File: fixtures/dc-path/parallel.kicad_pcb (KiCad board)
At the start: 2 copper layers, 2 parts

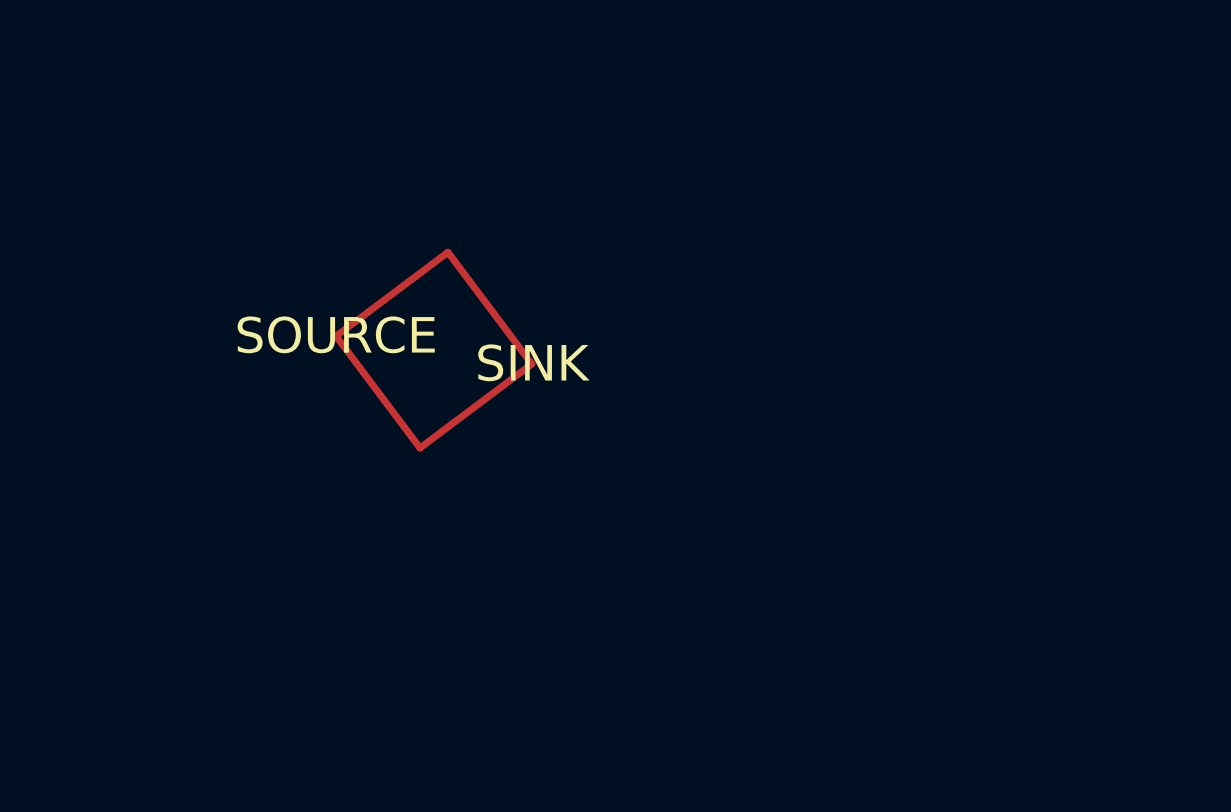
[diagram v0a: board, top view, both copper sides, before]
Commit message: Refuse DC copper outside qualified substrate and inventory footprint fields
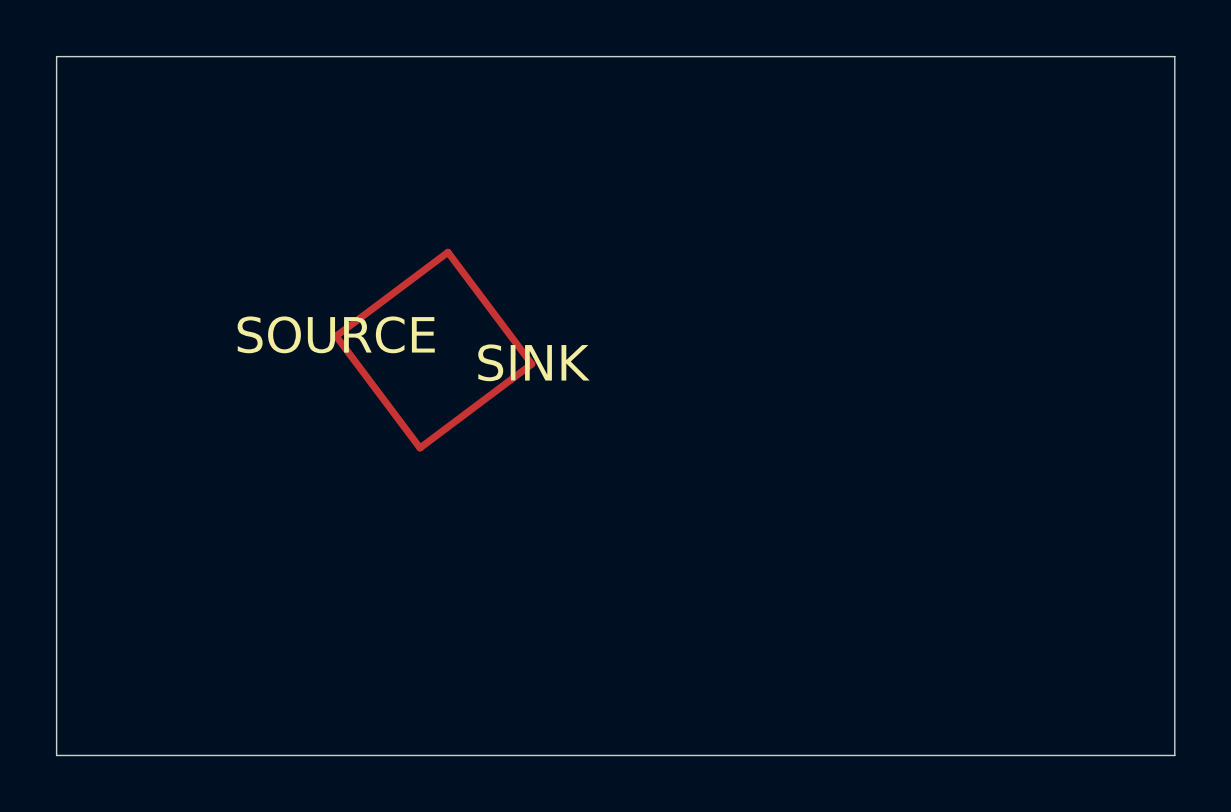
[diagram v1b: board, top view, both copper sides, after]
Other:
- board outline added: 40 x 25 mm
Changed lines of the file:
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@@
 		(embedded_fonts no)
+	)
+	(gr_line
+		(start 20 20)
+		(end 60 20)
+		(stroke
+			(width 0.05)
+			(type default)
+		)
+		(layer "Edge.Cuts")
+	)
+	(gr_line
+		(start 20 45)
+		(end 20 20)
+		(stroke
+			(width 0.05)
+			(type default)
+		)
+		(layer "Edge.Cuts")
+	)
+	(gr_line
+		(start 60 20)
+		(end 60 45)
+		(stroke
+			(width 0.05)
+			(type default)
+		)
+		(layer "Edge.Cuts")
+	)
+	(gr_line
+		(start 60 45)
+		(end 20 45)
+		(stroke
+			(width 0.05)
+			(type default)
+		)
+		(layer "Edge.Cuts")
 	)
 	(segment
